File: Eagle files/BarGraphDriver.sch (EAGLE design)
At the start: 32 parts, among them IC1 74HC595D, IC2 74HC595D

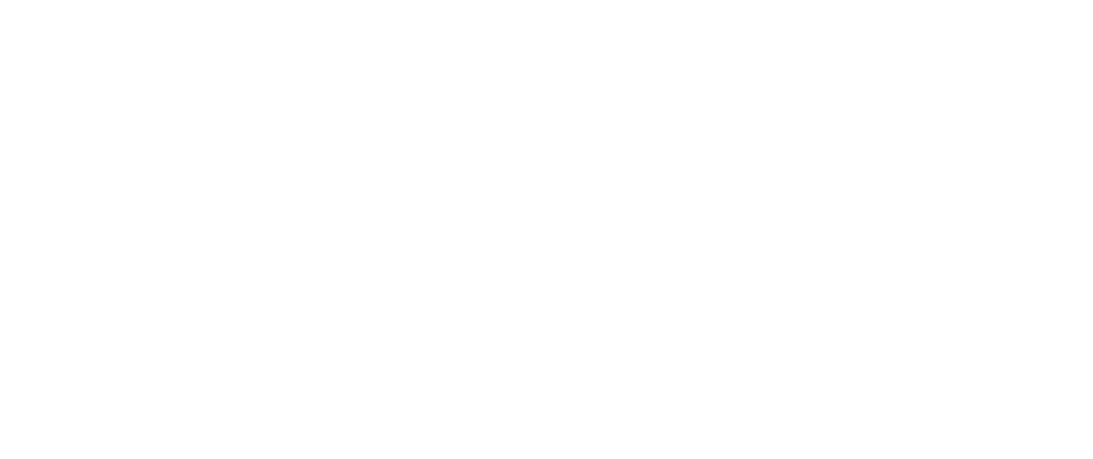
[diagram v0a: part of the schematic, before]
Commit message: Ready for Fabbing
Silk Screens added and last minute DRC checks done.
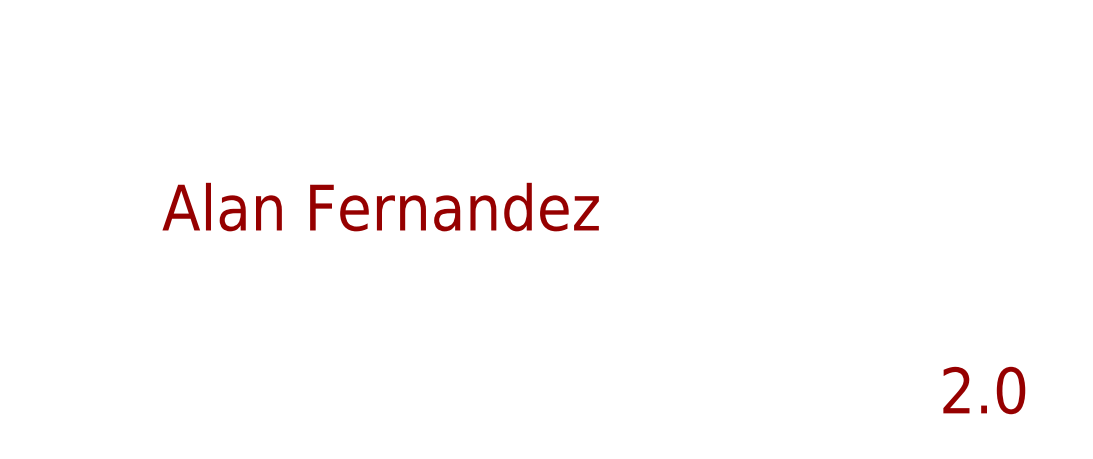
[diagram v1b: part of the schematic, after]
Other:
- note added: "2.0"
- note added: "Alan Fernandez"
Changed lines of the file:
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@@
 <part name="SER" library="wirepad" deviceset="WIREPAD" device="2,15/1,0" value="WIREPAD2,15/1,0"/>
 <part name="S_OUT" library="wirepad" deviceset="WIREPAD" device="2,15/1,0" value="WIREPAD2,15/1,0"/>
+<part name="FRAME1" library="frames" deviceset="LETTER_L" device=""/>
 </parts>
 <sheets>
 <sheet>
 <plain>
+<text x="66.04" y="-48.26" size="5.08" layer="94">Alan Fernandez</text>
+<text x="152.4" y="-68.58" size="5.08" layer="94">2.0</text>
 </plain>
 <instances>
@@
 <instance part="IC1" gate="P" x="27.94" y="68.58" rot="R270"/>
 <instance part="IC2" gate="P" x="27.94" y="73.66" rot="R270"/>
+<instance part="FRAME1" gate="G$1" x="-83.82" y="-73.66"/>
+<instance part="FRAME1" gate="G$2" x="63.5" y="-73.66"/>
 </instances>
 <busses>
